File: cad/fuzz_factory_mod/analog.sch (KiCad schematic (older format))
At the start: 8 parts

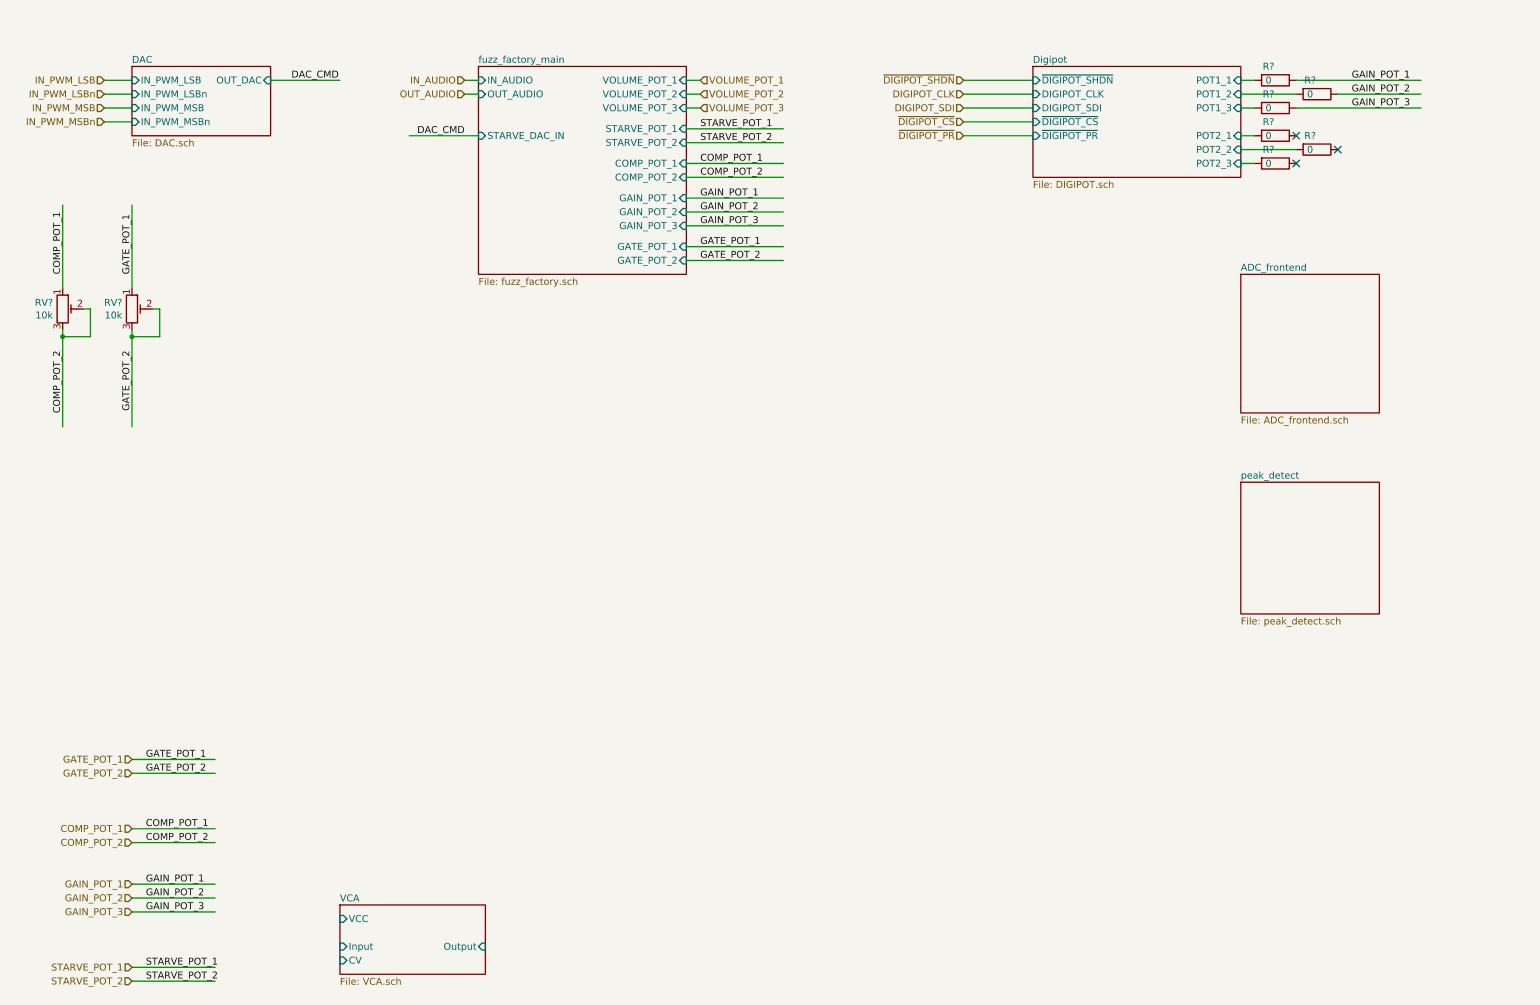
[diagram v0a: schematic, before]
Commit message: Modified OPA repartition on peak detector.
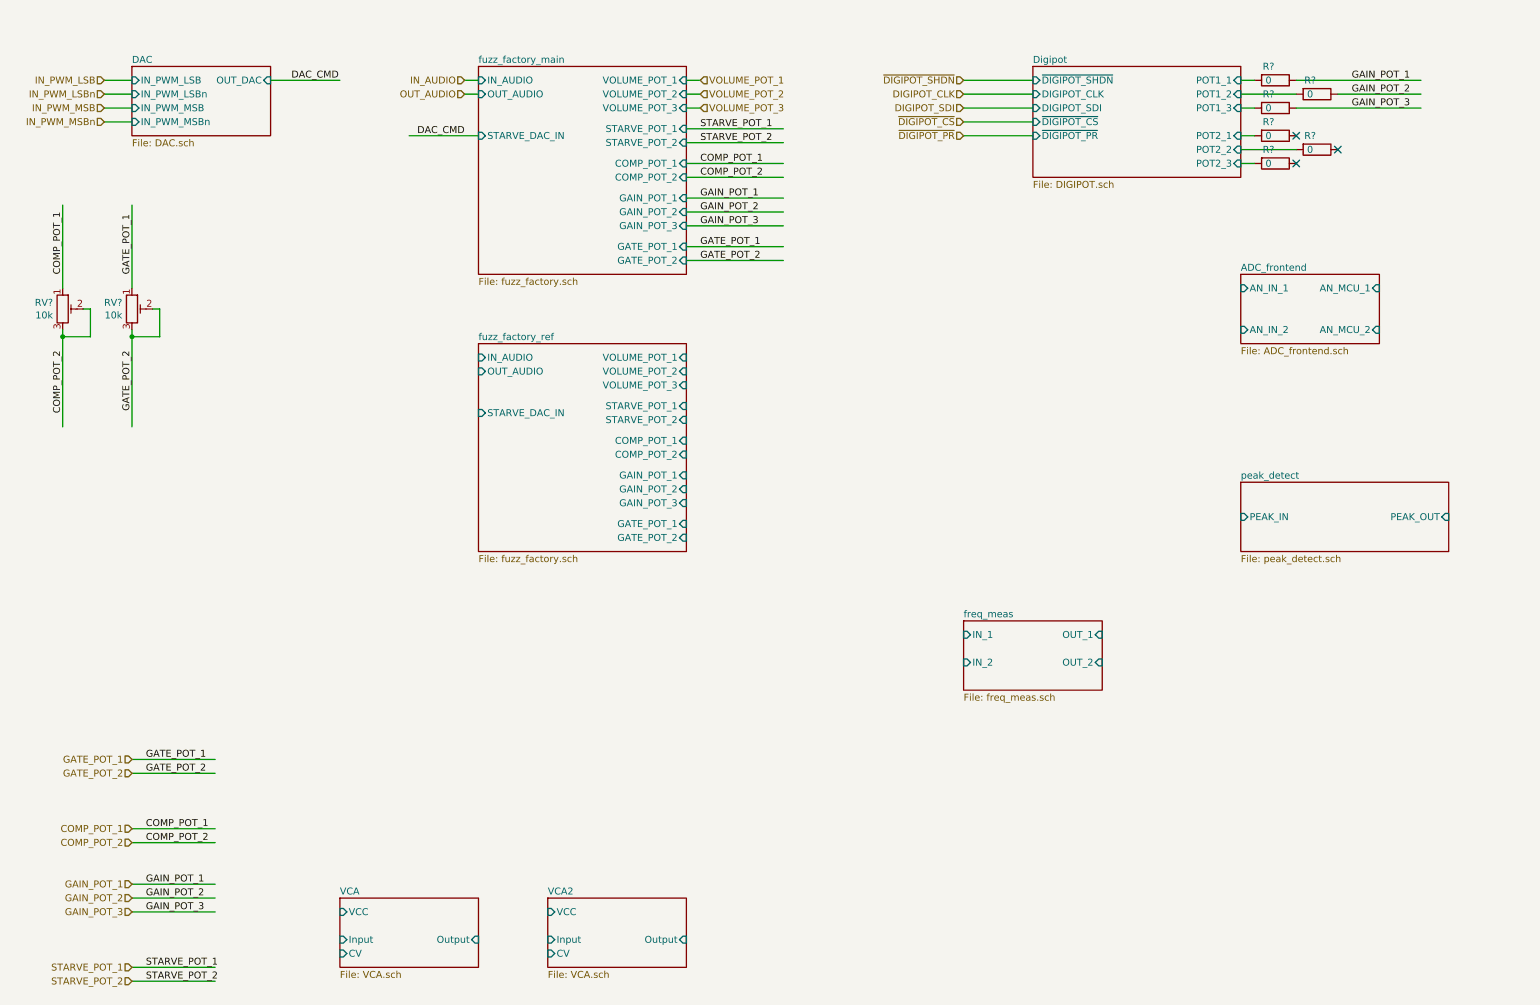
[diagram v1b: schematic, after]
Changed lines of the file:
@@
 $Descr A4 11693 8268
 encoding utf-8
-Sheet 3 16
+Sheet 3 19
 Title ""
 Date ""
@@
 NoConn ~ 9900 1700
 $Sheet
-S 3000 7050 1050 500
+S 3000 7000 1000 500
 U 5E344810
 F0 "VCA" 50
 F1 "VCA.sch" 50
-F2 "CV" I L 3000 7450 50
-F3 "Input" I L 3000 7350 50
-F4 "VCC" I L 3000 7150 50
-F5 "Output" I R 4050 7350 50
+F2 "CV" I L 3000 7400 50
+F3 "Input" I L 3000 7300 50
+F4 "VCC" I L 3000 7100 50
+F5 "Output" I R 4000 7300 50
 $EndSheet
 $Sheet
@@
 	5500 2400 6200 2400
 $Sheet
-S 9500 2500 1000 1000
+S 9500 2500 1000 500
 U 5E66F94D
 F0 "ADC_frontend" 50
 F1 "ADC_frontend.sch" 50
-$EndSheet
-$Sheet
-S 9500 4000 1000 950
+F2 "AN_IN_1" I L 9500 2600 50
+F3 "AN_MCU_1" I R 10500 2600 50
+F4 "AN_IN_2" I L 9500 2900 50
+F5 "AN_MCU_2" I R 10500 2900 50
+$EndSheet
+$Sheet
+S 9500 4000 1500 500
 U 5E68EE8E
 F0 "peak_detect" 50
 F1 "peak_detect.sch" 50
+F2 "PEAK_IN" I L 9500 4250 50
+F3 "PEAK_OUT" I R 11000 4250 50
+$EndSheet
+$Sheet
+S 7500 5000 1000 500
+U 5E6C0B65
+F0 "freq_meas" 50
+F1 "freq_meas.sch" 50
+F2 "IN_1" I L 7500 5100 50
+F3 "OUT_1" I R 8500 5100 50
+F4 "IN_2" I L 7500 5300 50
+F5 "OUT_2" I R 8500 5300 50
+$EndSheet
+$Sheet
+S 4500 7000 1000 500
+U 5E6FC466
+F0 "VCA2" 50
+F1 "VCA.sch" 50
+F2 "CV" I L 4500 7400 50
+F3 "Input" I L 4500 7300 50
+F4 "VCC" I L 4500 7100 50
+F5 "Output" I R 5500 7300 50
+$EndSheet
+$Sheet
+S 4000 3000 1500 1500
+U 5E6FFBAD
+F0 "fuzz_factory_ref" 50
+F1 "fuzz_factory.sch" 50
+F2 "VOLUME_POT_1" I R 5500 3100 50
+F3 "VOLUME_POT_2" I R 5500 3200 50
+F4 "VOLUME_POT_3" I R 5500 3300 50
+F5 "IN_AUDIO" I L 4000 3100 50
+F6 "OUT_AUDIO" I L 4000 3200 50
+F7 "STARVE_DAC_IN" I L 4000 3500 50
+F8 "STARVE_POT_1" I R 5500 3450 50
+F9 "STARVE_POT_2" I R 5500 3550 50
+F10 "COMP_POT_1" I R 5500 3700 50
+F11 "COMP_POT_2" I R 5500 3800 50
+F12 "GAIN_POT_1" I R 5500 3950 50
+F13 "GAIN_POT_2" I R 5500 4050 50
+F14 "GAIN_POT_3" I R 5500 4150 50
+F15 "GATE_POT_1" I R 5500 4300 50
+F16 "GATE_POT_2" I R 5500 4400 50
 $EndSheet
 $EndSCHEMATC

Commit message: Continued schematic.
Modified fuuz_factory circuit : use of matched transistor pairs.
Added USB interface, through FT230X and direct to MCU.
Associated footprints, except for XTAL and trimmers.
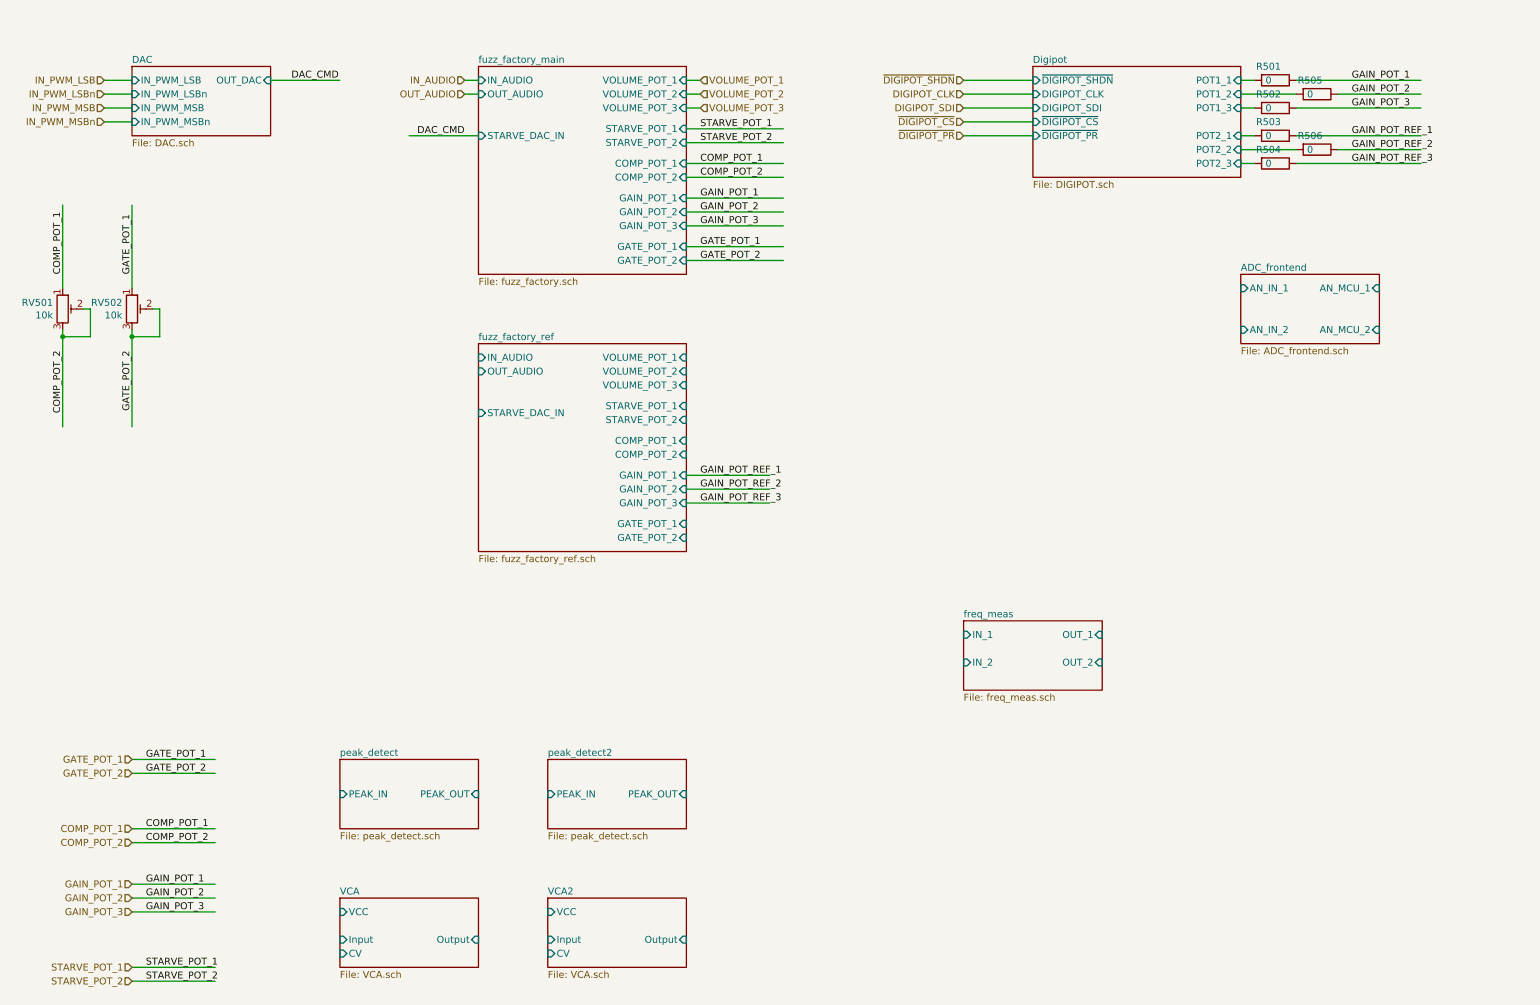
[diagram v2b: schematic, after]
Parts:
- R501, R502, R503, R504, R505, R506: renamed from R?; footprint (none) -> Resistors_SMD:R_0603
- gave numbers to parts that had none: 2
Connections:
- net labels added: GAIN_POT_REF_1, GAIN_POT_REF_2, GAIN_POT_REF_3
- wire segments 55 -> 61
- no-connect marks 3 -> 0
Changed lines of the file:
@@
 $Descr A4 11693 8268
 encoding utf-8
-Sheet 3 19
+Sheet 5 22
 Title ""
 Date ""
@@
 GATE_POT_2
 $Comp
-L Device:R_POT_TRIM RV?
+L Device:R_POT_TRIM RV501
 U 1 1 5DF4B057
 P 1000 2750
-F 0 "RV?" H 930 2796 50  0000 R CNN
+F 0 "RV501" H 930 2796 50  0000 R CNN
 F 1 "10k" H 930 2705 50  0000 R CNN
 F 2 "" H 1000 2750 50  0001 C CNN
@@
 COMP_POT_2
 $Comp
-L Device:R_POT_TRIM RV?
+L Device:R_POT_TRIM RV502
 U 1 1 5DF95B54
 P 1500 2750
-F 0 "RV?" H 1430 2796 50  0000 R CNN
+F 0 "RV502" H 1430 2796 50  0000 R CNN
 F 1 "10k" H 1430 2705 50  0000 R CNN
 F 2 "" H 1500 2750 50  0001 C CNN
@@
 	7500 1500 8000 1500
 $Comp
-L Device:R R?
+L Device:R R501
 U 1 1 5E37400A
 P 9750 1100
-F 0 "R?" V 9650 1050 50  0000 C CNN
+F 0 "R501" V 9650 1050 50  0000 C CNN
 F 1 "0" V 9750 1050 50  0000 C CNN
-F 2 "" V 9680 1100 50  0001 C CNN
+F 2 "Resistors_SMD:R_0603" V 9680 1100 50  0001 C CNN
 F 3 "~" H 9750 1100 50  0001 C CNN
 	1    9750 1100
@@
 $EndComp
 $Comp
-L Device:R R?
+L Device:R R505
 U 1 1 5E374C21
 P 10050 1200
-F 0 "R?" V 9950 1150 50  0000 C CNN
+F 0 "R505" V 9950 1150 50  0000 C CNN
 F 1 "0" V 10050 1150 50  0000 C CNN
-F 2 "" V 9980 1200 50  0001 C CNN
+F 2 "Resistors_SMD:R_0603" V 9980 1200 50  0001 C CNN
 F 3 "~" H 10050 1200 50  0001 C CNN
 	1    10050 1200
@@
 $EndComp
 $Comp
-L Device:R R?
+L Device:R R502
 U 1 1 5E3751A9
 P 9750 1300
-F 0 "R?" V 9650 1250 50  0000 C CNN
+F 0 "R502" V 9650 1250 50  0000 C CNN
 F 1 "0" V 9750 1250 50  0000 C CNN
-F 2 "" V 9680 1300 50  0001 C CNN
+F 2 "Resistors_SMD:R_0603" V 9680 1300 50  0001 C CNN
 F 3 "~" H 9750 1300 50  0001 C CNN
 	1    9750 1300
@@
 $EndComp
 $Comp
-L Device:R R?
+L Device:R R503
 U 1 1 5E376867
 P 9750 1500
-F 0 "R?" V 9650 1450 50  0000 C CNN
+F 0 "R503" V 9650 1450 50  0000 C CNN
 F 1 "0" V 9750 1450 50  0000 C CNN
-F 2 "" V 9680 1500 50  0001 C CNN
+F 2 "Resistors_SMD:R_0603" V 9680 1500 50  0001 C CNN
 F 3 "~" H 9750 1500 50  0001 C CNN
 	1    9750 1500
@@
 $EndComp
 $Comp
-L Device:R R?
+L Device:R R506
 U 1 1 5E376871
 P 10050 1600
-F 0 "R?" V 9950 1550 50  0000 C CNN
+F 0 "R506" V 9950 1550 50  0000 C CNN
 F 1 "0" V 10050 1550 50  0000 C CNN
-F 2 "" V 9980 1600 50  0001 C CNN
+F 2 "Resistors_SMD:R_0603" V 9980 1600 50  0001 C CNN
 F 3 "~" H 10050 1600 50  0001 C CNN
 	1    10050 1600
@@
 $EndComp
 $Comp
-L Device:R R?
+L Device:R R504
 U 1 1 5E37687B
 P 9750 1700
-F 0 "R?" V 9650 1650 50  0000 C CNN
+F 0 "R504" V 9650 1650 50  0000 C CNN
 F 1 "0" V 9750 1650 50  0000 C CNN
-F 2 "" V 9680 1700 50  0001 C CNN
+F 2 "Resistors_SMD:R_0603" V 9680 1700 50  0001 C CNN
 F 3 "~" H 9750 1700 50  0001 C CNN
 	1    9750 1700
@@
 Wire Wire Line
 	9900 1300 10800 1300
-NoConn ~ 9900 1500
-NoConn ~ 10200 1600
-NoConn ~ 9900 1700
 $Sheet
 S 3000 7000 1000 500
@@
 $EndSheet
 $Sheet
-S 9500 4000 1500 500
+S 3000 6000 1000 500
 U 5E68EE8E
 F0 "peak_detect" 50
 F1 "peak_detect.sch" 50
-F2 "PEAK_IN" I L 9500 4250 50
-F3 "PEAK_OUT" I R 11000 4250 50
+F2 "PEAK_IN" I L 3000 6250 50
+F3 "PEAK_OUT" I R 4000 6250 50
 $EndSheet
 $Sheet
@@
 $EndSheet
 $Sheet
+S 4500 6000 1000 500
+U 5EB8346E
+F0 "peak_detect2" 50
+F1 "peak_detect.sch" 50
+F2 "PEAK_IN" I L 4500 6250 50
+F3 "PEAK_OUT" I R 5500 6250 50
+$EndSheet
+$Sheet
 S 4000 3000 1500 1500
-U 5E6FFBAD
+U 5EB9A4D1
 F0 "fuzz_factory_ref" 50
-F1 "fuzz_factory.sch" 50
+F1 "fuzz_factory_ref.sch" 50
 F2 "VOLUME_POT_1" I R 5500 3100 50
 F3 "VOLUME_POT_2" I R 5500 3200 50
@@
 F16 "GATE_POT_2" I R 5500 4400 50
 $EndSheet
+Text Label 10300 1500 0    50   ~ 0
+GAIN_POT_REF_1
+Text Label 10300 1600 0    50   ~ 0
+GAIN_POT_REF_2
+Text Label 10300 1700 0    50   ~ 0
+GAIN_POT_REF_3
+Wire Wire Line
+	9900 1500 10800 1500
+Wire Wire Line
+	10200 1600 10800 1600
+Wire Wire Line
+	9900 1700 10800 1700
+Text Label 5600 3950 0    50   ~ 0
+GAIN_POT_REF_1
+Text Label 5600 4050 0    50   ~ 0
+GAIN_POT_REF_2
+Text Label 5600 4150 0    50   ~ 0
+GAIN_POT_REF_3
+Wire Wire Line
+	5500 4050 6100 4050
+Wire Wire Line
+	6100 3950 5500 3950
+Wire Wire Line
+	5500 4150 6100 4150
 $EndSCHEMATC

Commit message: Continued schematic.
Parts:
- added C501: 100n, Capacitors_SMD:C_0603, symbol Device:C
- added R507: 100k, Resistors_SMD:R_0603, symbol Device:R
- added R508: 0, Resistors_SMD:R_0603, symbol Device:R
- added R509: 10k, Resistors_SMD:R_0603, symbol Device:R
- added RV503, RV504: 10k, Potentiometers:Potentiometer_Trimmer_Bourns_3266X, symbol Device:R_POT_TRIM
- RV501, RV502: footprint (none) -> Potentiometers:Potentiometer_Trimmer_Bourns_3266X
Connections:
- net labels added: +3.3V, +9V, COMP_POT_REF_1, COMP_POT_REF_2, DAC_CMD_1, DAC_CMD_2, FF_Stab_DAC_PWM_LSB, FF_Stab_DAC_PWM_MSB, GATE_POT_REF_1, GATE_POT_REF_2, GNDA, IN_AUDIO_FREQ, IN_AUDIO_PEAK, IN_AUDIO_VCA, IN_AUDIO_VCA_PEAK, OUT_AUDIO_PEAK, OUT_AUDIO_REF, OUT_AUDIO_REF_FREQ, OUT_AUDIO_VCA, OUT_AUDIO_VCA_FREQ, OUT_AUDIO_VCA_PEAK, Ref_Stab_DAC_PWM_LSB, Ref_Stab_DAC_PWM_MSB, SPI_FF_Gain_CS, SPI_FF_Gain_MISO, SPI_FF_Gain_SCK, VCA_IN_PWM, VCA_OUT_PWM, VOLUME_POT_REF_1, VOLUME_POT_REF_2, VOLUME_POT_REF_3
- net labels removed: DAC_CMD, DIGIPOT_CLK, DIGIPOT_SDI, IN_PWM_LSB, IN_PWM_LSBn, IN_PWM_MSB, IN_PWM_MSBn, ~DIGIPOT_CS, ~DIGIPOT_PR, ~DIGIPOT_SHDN
- wire segments 61 -> 112
- no-connect marks 0 -> 12
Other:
- moved on the sheet: R501, R502, R503, R504, R505, R506, RV501, RV502
